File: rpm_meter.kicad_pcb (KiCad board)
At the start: 2 copper layers, 153.8 x 95.2 mm, 112 parts, among them IC1 SN74LV1T34DCKR, IC6 TPS566247DRLR, J1 Conn_01x01_Socket, J2 Conn_2Rows-05Pins, J3 Conn_01x01_Socket, J4 Conn_01x01_Socket, J5 Conn_01x01_Socket, J6 Conn_01x01_Socket, J7 Conn_01x01_Socket, Q1 BC846, Q14 BC846, Q15 BC846, Q16 BC846, U1 M24C02-RMN, U2 STM32C031C6Tx, U3 74LVC1G123, U4 TLV1117-33, U5 PEC11R-4225F-S0024, Y1 8

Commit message: Encoder
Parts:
- removed U5: PEC11R-4225F-S0024, Library_local:PEC12R-4XXXF-SXXXX_1
- added C18: 100n, Capacitor_SMD:C_0603_1608Metric, F.Cu at (214.6, 89.7)
- added C19: 100n, Capacitor_SMD:C_0603_1608Metric, F.Cu at (201.1, 76.5)
- added C20: 100n, Capacitor_SMD:C_0603_1608Metric, F.Cu at (204.2, 76.5)
- added R10: 10k, Resistor_SMD:R_0603_1608Metric, F.Cu at (195.1, 89.6)
- added R11: 10k, Resistor_SMD:R_0603_1608Metric, F.Cu at (214.6, 86.5)
- added R12: 1k, Resistor_SMD:R_0603_1608Metric, F.Cu at (195.1, 83.5)
- added R13: 1k, Resistor_SMD:R_0603_1608Metric, F.Cu at (195.1, 86.5)
- added R16: 1k, Resistor_SMD:R_0603_1608Metric, F.Cu at (214.6, 83.4)
- added R8: 10k, Resistor_SMD:R_0603_1608Metric, F.Cu at (195.1, 80.4)
- added SW1: RotaryEncoder_Switch_MP, Library_local:RotaryEncoder_Alps_EC12E-Switch_Vertical_H20mm, F.Cu at (197.6, 82.7)

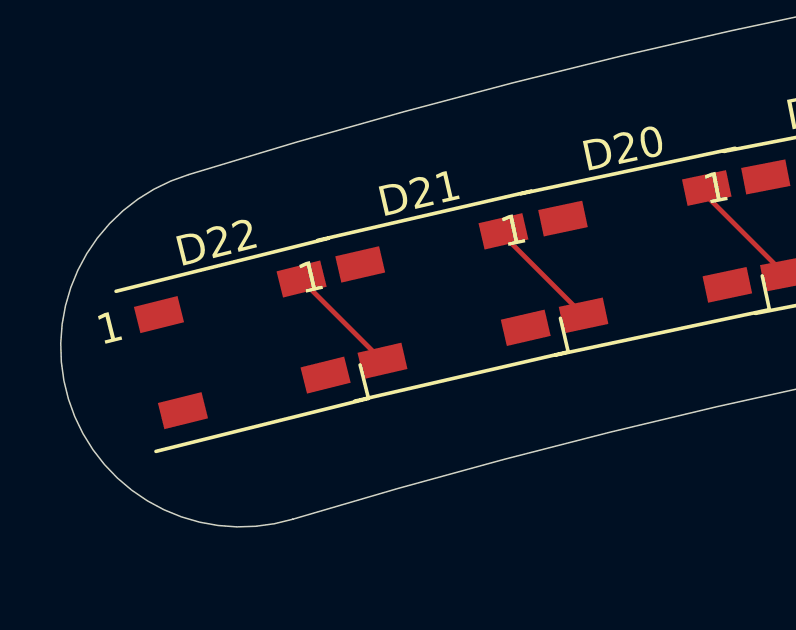
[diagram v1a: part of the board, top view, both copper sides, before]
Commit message: Add optional leds end resistors
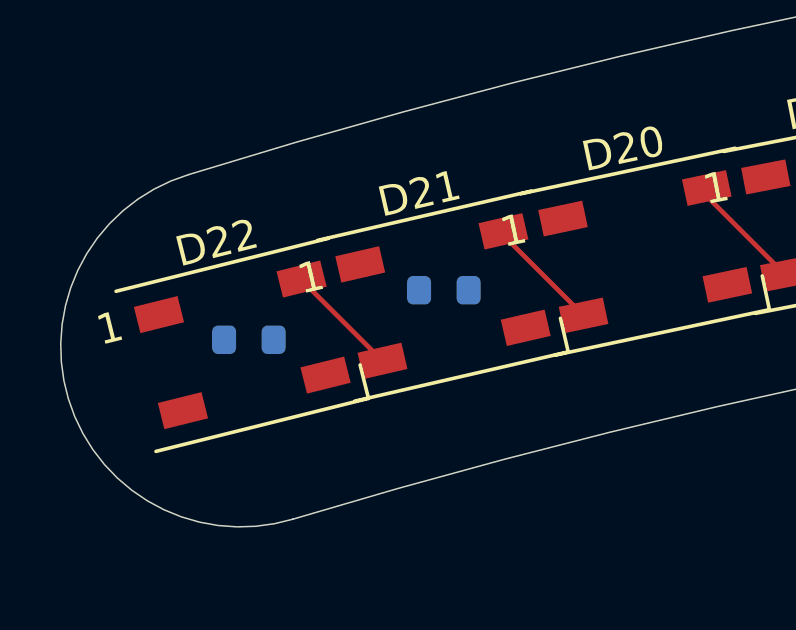
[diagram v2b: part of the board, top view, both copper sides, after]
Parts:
- added R17: 10k, Resistor_SMD:R_0603_1608Metric, B.Cu at (74.4, 45.2)
- added R18: 10k, Resistor_SMD:R_0603_1608Metric, B.Cu at (80.9, 43.6)
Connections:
- D22 pad 2: unconnected-(D22-DOUT-Pad2) -> Net-(D22-DOUT)

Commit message: 2.1
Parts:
- added C21: 100n, Capacitor_SMD:C_0603_1608Metric, B.Cu at (73.2, 47.4)
- added C29: 100n, Capacitor_SMD:C_0603_1608Metric, B.Cu at (100.3, 38.6)
- added C30: 100n, Capacitor_SMD:C_0603_1608Metric, B.Cu at (128.6, 34.5)
- added C31: 100n, Capacitor_SMD:C_0603_1608Metric, B.Cu at (135.7, 34.2)
- added C32: 100n, Capacitor_SMD:C_0603_1608Metric, B.Cu at (142.8, 34.2)
- added C33: 100n, Capacitor_SMD:C_0603_1608Metric, B.Cu at (79.9, 45.2)
- added C34: 100n, Capacitor_SMD:C_0603_1608Metric, B.Cu at (107.2, 37.3)
- added C35: 100n, Capacitor_SMD:C_0603_1608Metric, B.Cu at (157.1, 35.2)
- added C36: 100n, Capacitor_SMD:C_0603_1608Metric, B.Cu at (164.2, 36.0)
- added C37: 100n, Capacitor_SMD:C_0603_1608Metric, B.Cu at (150.0, 34.6)
- added C38: 100n, Capacitor_SMD:C_0603_1608Metric, B.Cu at (86.6, 42.6)
- added C39: 100n, Capacitor_SMD:C_0603_1608Metric, B.Cu at (114.3, 36.0)
- added C40: 100n, Capacitor_SMD:C_0603_1608Metric, B.Cu at (171.2, 37.1)
- added C41: 100n, Capacitor_SMD:C_0603_1608Metric, B.Cu at (178.2, 38.6)
- added C42: 100n, Capacitor_SMD:C_0603_1608Metric, B.Cu at (185.1, 40.4)
- added C43: 100n, Capacitor_SMD:C_0603_1608Metric, B.Cu at (93.4, 40.6)
- added C44: 100n, Capacitor_SMD:C_0603_1608Metric, B.Cu at (121.4, 35.2)
- added C45: 100n, Capacitor_SMD:C_0603_1608Metric, B.Cu at (191.9, 42.5)
- added C46: 100n, Capacitor_SMD:C_0603_1608Metric, B.Cu at (198.2, 44.8)
- added C47: 100n, Capacitor_SMD:C_0603_1608Metric, F.Cu at (205.1, 49.9)
- C3, R52, R53, R54, R67, U1: moved to F.Cu
- D10, D11, D12, D13, D14, D15, D16, D17, D18, D19, D20, D21, D22, D3, D4, D5, D6, D7, D8, D9: footprint LED_SMD:LED_WS2812B_PLCC4_5.0x5.0mm_P3.2mm -> Library_local:LED_WS2812B-2020_PLCC4_2.0x2.0mm
- D2, D23, D24, D26: moved to B.Cu
- Y1: footprint Crystal:Crystal_SMD_3225-4Pin_3.2x2.5mm -> Crystal:Crystal_SMD_2520-4Pin_2.5x2.0mm
- moved C10 39.2 mm to (218.6, 76.0), turned to 180 degrees
- moved Q14 37.5 mm to (215.3, 74.2)
- moved R62 37.4 mm to (219.4, 73.8), turned to -90 degrees
- moved R61 35.5 mm to (217.8, 73.8)
- moved D24 28.7 mm to (222.1, 101.3)
- moved R2 27.9 mm to (209.5, 95.9), turned to 180 degrees
- moved D26 26.1 mm to (225.7, 101.3), turned to -90 degrees
- moved J7 22.8 mm to (228.5, 119.0)
- moved R54 22.5 mm to (197.2, 65.3), turned to -90 degrees
- moved R53 21.2 mm to (200.4, 65.3), turned to -90 degrees
- moved D23 21.0 mm to (221.3, 117.0), turned to -90 degrees
- moved R73 20.7 mm to (209.5, 94.3)
- moved D25 20.3 mm to (218.3, 98.2), turned to -90 degrees
- moved R60 20.0 mm to (219.4, 117.3)
- moved C9 19.8 mm to (221.8, 115.0), turned to 180 degrees
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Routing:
- net Net-(D4-DOUT): track 4.45 -> 0.00 mm
- net Net-(D10-DOUT): track 4.21 -> 0.00 mm
- net Net-(D8-DOUT): track 4.19 -> 0.00 mm
- net Net-(D10-DIN): track 4.16 -> 0.00 mm
- net Net-(D7-DOUT): track 4.15 -> 0.00 mm
- net Net-(D3-DOUT): track 4.13 -> 0.00 mm
- net Net-(D11-DOUT): track 4.13 -> 0.00 mm
- net Net-(D6-DOUT): track 4.12 -> 0.00 mm
- net Net-(D5-DOUT): track 4.11 -> 0.00 mm
- net Net-(D12-DOUT): track 4.09 -> 0.00 mm
- net Net-(D14-DOUT): track 4.00 -> 0.00 mm
- net Net-(D17-DOUT): track 3.98 -> 0.00 mm
- net Net-(D18-DOUT): track 3.96 -> 0.00 mm
- net Net-(D19-DOUT): track 3.95 -> 0.00 mm
- net Net-(D16-DOUT): track 3.95 -> 0.00 mm
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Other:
- board size 153.8 x 95.2 mm -> 170.4 x 98.7 mm

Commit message: v2.1
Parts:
- added REF**: MountingHole_3.2mm_M3_ISO14580, MountingHole:MountingHole_3.2mm_M3_ISO14580, B.Cu at (221.2, 122.2)
- added REF**: MountingHole_3.2mm_M3_ISO14580, MountingHole:MountingHole_3.2mm_M3_ISO14580, B.Cu at (199.7, 95.6)
- added REF**: MountingHole_3.2mm_M3_ISO14580, MountingHole:MountingHole_3.2mm_M3_ISO14580, B.Cu at (215.3, 51.2)
- added REF**: MountingHole_3.2mm_M3_ISO14580, MountingHole:MountingHole_3.2mm_M3_ISO14580, B.Cu at (63.1, 51.2)
- C47: moved to B.Cu
- moved TP5 21.1 mm to (218.8, 65.8)
- moved JP1 13.3 mm to (203.2, 56.5), turned to 0 degrees
- moved Y1 11.4 mm to (207.4, 67.2)
- moved C4 9.56 mm to (195.2, 60.0)
- moved C5 9.56 mm to (193.6, 60.0)
- moved C6 9.56 mm to (200.2, 60.0)
- moved C7 9.56 mm to (196.8, 60.0)
- moved C8 9.56 mm to (198.5, 60.0)
- moved IC1 8.39 mm to (206.6, 55.5)
- moved R72 7.53 mm to (224.3, 101.7)
- moved R1 7.50 mm to (220.3, 101.7)
- moved D26 7.42 mm to (223.7, 94.2)
- moved D24 7.38 mm to (220.1, 94.2)
- moved D2 6.20 mm to (224.9, 110.8)
- moved D23 6.15 mm to (221.2, 110.8)
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
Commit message: connections 1.0
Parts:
- moved TP4 21.7 mm to (218.7, 83.3)
- moved JP1 6.90 mm to (208.3, 51.9), turned to 180 degrees
- moved TP3 6.43 mm to (207.9, 101.7)
- moved J1 6.22 mm to (228.8, 120.6)
- moved J5 4.70 mm to (224.4, 124.9)
- moved J7 4.35 mm to (229.1, 124.8)
- moved J3 3.04 mm to (225.9, 122.0)
- moved J6 2.15 mm to (226.6, 124.9)
- moved R53 1.60 mm to (196.8, 69.8)
- moved R52 1.57 mm to (198.4, 69.8)
- turned D2 to -90 degrees
- turned R68 to 90 degrees
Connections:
- U2 pad 39: /mcu/led_pwm_out_3v3 -> /Leds/WS2812B_IN
- U2 pad 44: /mcu/SPI_MOSI -> unconnected-(U2-PB5-Pad44)
- U2 pad 45: /mcu/SPI_SCK -> unconnected-(U2-PB6-Pad45)
- U2 pad 46: /mcu/LATCH_PIN -> unconnected-(U2-PB7-Pad46)
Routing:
- net +5V: track 0.00 -> 225.3 mm, vias 0 -> 20
- net GND: track 0.00 -> 84.1 mm, vias 0 -> 3
- net +3.3V: track 0.00 -> 51.2 mm
- net /alert_yellow/12v_signal: track 0.00 -> 34.8 mm
- net /alert_red/12v_signal: track 0.00 -> 32.9 mm
- net /light/12v_signal: track 0.00 -> 30.1 mm
- net Net-(D27-K): track 0.00 -> 25.7 mm, vias 0 -> 1
- net Net-(D24-A2): track 0.00 -> 21.7 mm, vias 0 -> 1
- net Net-(D26-A2): track 0.00 -> 20.6 mm, vias 0 -> 1
- net Net-(D25-A2): track 0.00 -> 14.7 mm, vias 0 -> 1
- net Net-(D2-A2): track 0.00 -> 14.6 mm, vias 0 -> 1
- net Net-(IC6-VIN): track 0.00 -> 14.5 mm
- net Net-(D3-DOUT): track 0.00 -> 14.5 mm
- net Net-(IC6-FB): track 0.00 -> 12.6 mm, vias 0 -> 2
- net /rpm_signal/rpm_signal: track 0.00 -> 12.4 mm
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
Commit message: Connections 1.1
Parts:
- moved R73 3.23 mm to (209.5, 97.5)
- moved R67 1.62 mm to (209.5, 95.9)
- moved R2 1.55 mm to (209.5, 94.3)
- moved R12 0.36 mm to (197.0, 84.4)
- moved R8 0.35 mm to (197.0, 81.3)
- moved R13 0.33 mm to (197.0, 87.5)
- moved R10 0.30 mm to (196.9, 90.7)
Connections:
- TP3 pad 1: Net-(D27-K) -> Net-(Q14-B)
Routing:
- net Net-(D26-A2): track 20.6 -> 70.5 mm
- net Net-(Q14-B): track 0.00 -> 48.4 mm, vias 0 -> 2
- net Net-(D24-A2): track 21.7 -> 65.0 mm
- net Net-(D25-A2): track 14.7 -> 56.3 mm
- net Net-(D27-K): track 25.7 -> 8.39 mm, vias 1 -> 0
- net +3.3V: track 51.2 -> 63.7 mm
- net GND: track 84.1 -> 89.6 mm

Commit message: routing2.0
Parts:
- moved C5 13.4 mm to (206.5, 63.7)
- moved C4 11.6 mm to (206.8, 60.3), turned to -90 degrees
- moved C3 5.00 mm to (196.9, 60.0), turned to 90 degrees
- moved C7 3.43 mm to (200.2, 60.0), turned to -90 degrees
- moved C6 1.69 mm to (201.8, 60.0), turned to 90 degrees
- moved U3 0.20 mm to (212.4, 68.0)
- moved C8 0.06 mm to (198.5, 60.0), turned to -90 degrees
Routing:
- net +3.3V: track 63.7 -> 164.6 mm, vias 0 -> 8
- net +5V: track 225.3 -> 282.5 mm, vias 20 -> 21
- net /mcu/enc_p: track 0.00 -> 43.5 mm
- net /mcu/enc_a: track 0.00 -> 43.1 mm, vias 0 -> 2
- net Net-(Q16-C): track 0.00 -> 35.6 mm, vias 0 -> 2
- net /mcu/enc_b: track 0.00 -> 33.1 mm, vias 0 -> 2
- net GND: track 89.6 -> 121.2 mm, vias 3 -> 23
- net /mcu/NRST: track 0.00 -> 29.3 mm, vias 0 -> 2
- net Net-(Q15-C): track 0.00 -> 28.9 mm, vias 0 -> 2
- net /mcu/scl: track 4.40 -> 28.4 mm, vias 0 -> 2
- net Net-(Q1-C): track 0.00 -> 23.8 mm
- net /mcu/sda: track 2.20 -> 25.6 mm, vias 0 -> 2
- net /mcu/TMS: track 0.00 -> 21.6 mm, vias 0 -> 1
- net /mcu/rpm_signal_mcu: track 0.00 -> 20.5 mm, vias 0 -> 2
- net /mcu/TCK: track 0.00 -> 20.3 mm
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- added copper zone on B.Cu, net GND
- added copper zone on F.Cu, net GND

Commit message: routing2.1
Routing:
- net +3.3V: track 164.6 -> 185.3 mm, vias 8 -> 9
- net GND: track 121.2 -> 116.8 mm, vias 23 -> 33
